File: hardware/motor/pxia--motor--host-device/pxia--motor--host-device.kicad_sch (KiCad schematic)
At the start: 12 parts, among them J1 RJ45, J2 Lolin D32 Pro 2.0.0 (ESP32) P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, J3 GENERIC_UART, J4 Lolin D32 Pro 2.0.0 (ESP32) P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, U1 Teensy4.0, U2 max3490eesa+T

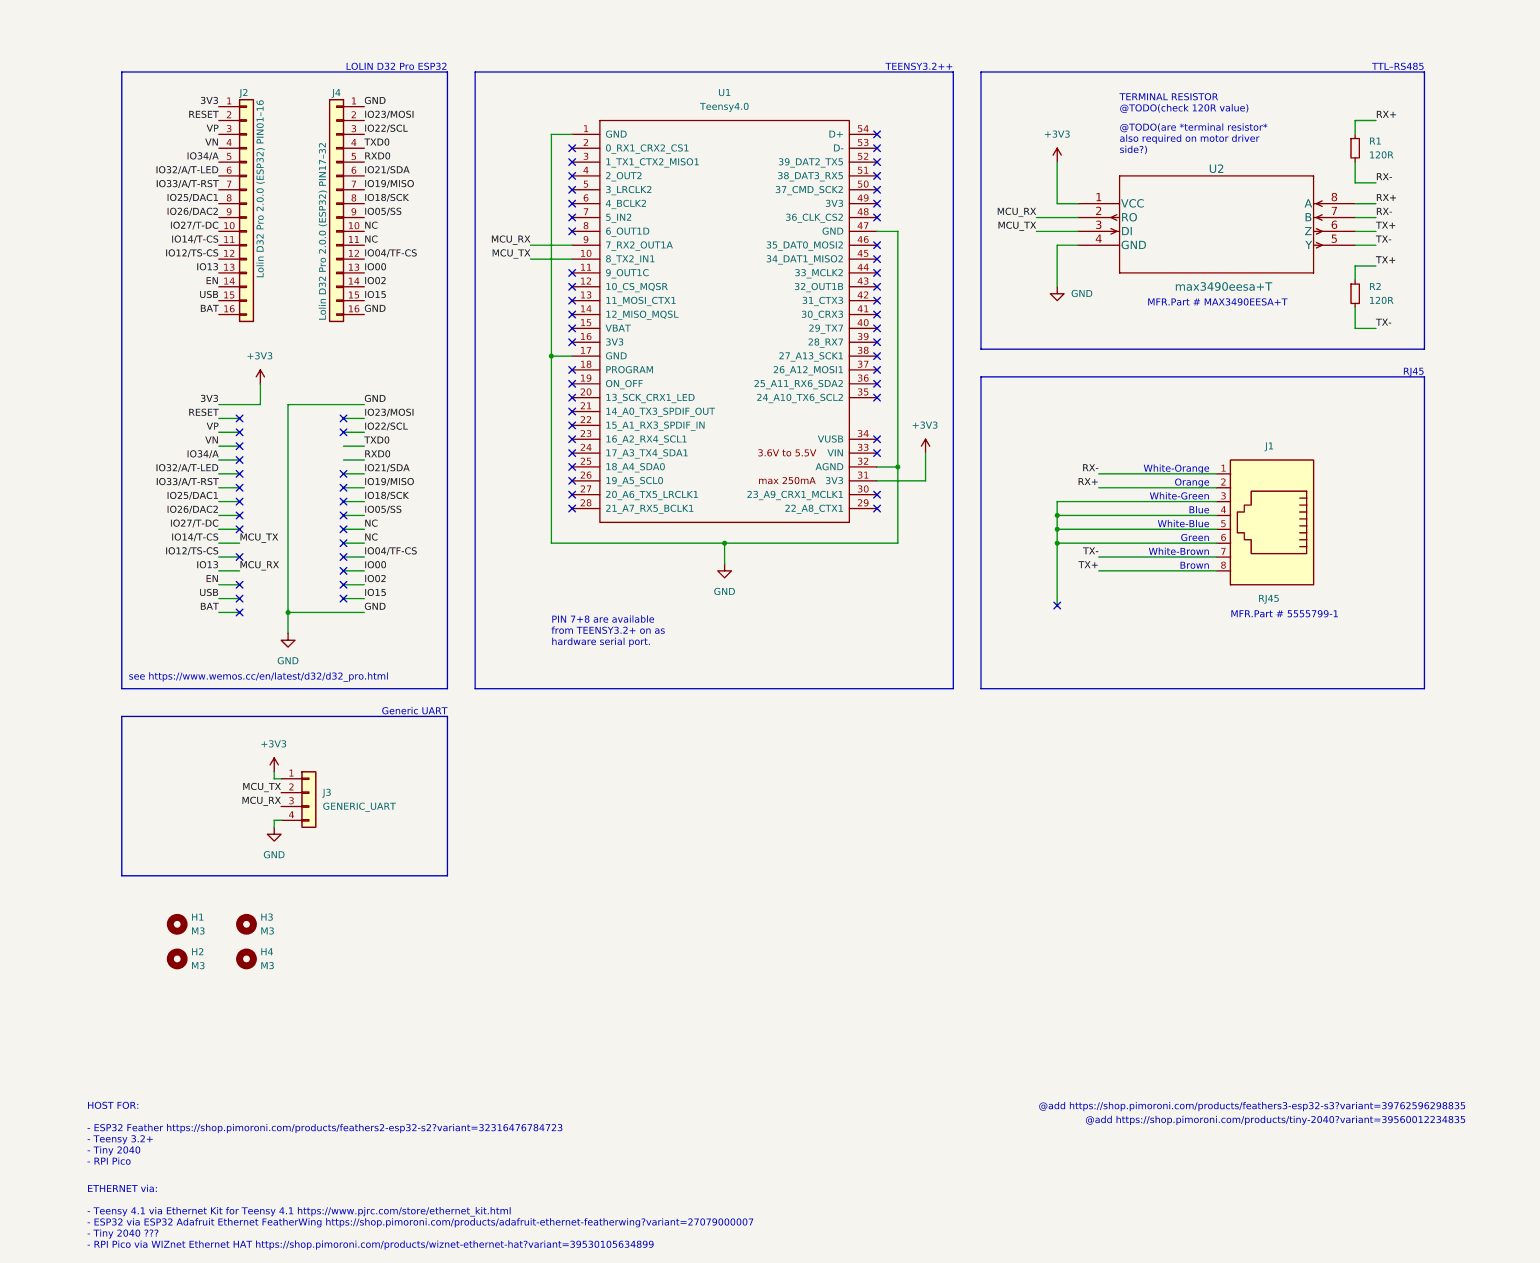
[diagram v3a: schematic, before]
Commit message: added PicoW, finished PCB layout
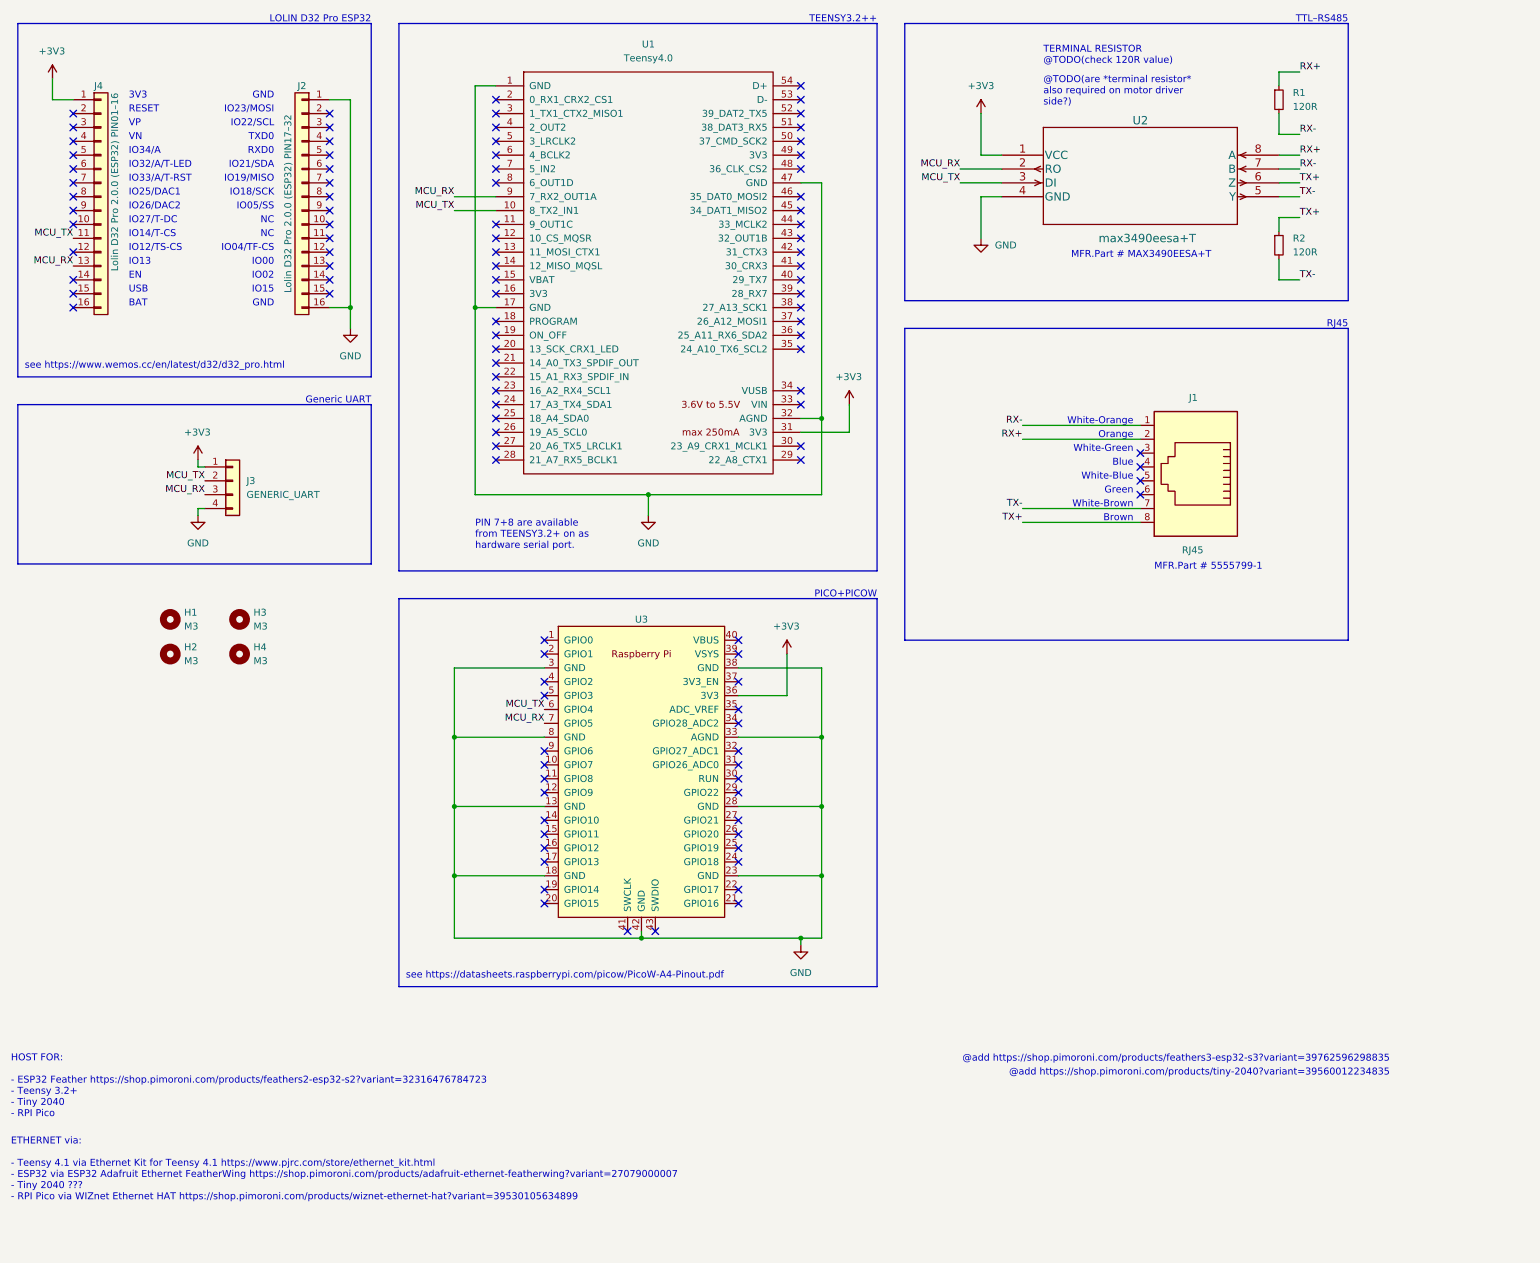
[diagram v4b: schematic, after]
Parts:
- added U3: (no value), symbol PicoW:PicoW
- J2: value Lolin D32 Pro 2.0.0 (ESP32) PIN01–16 -> Lolin D32 Pro 2.0.0 (ESP32) PIN17–32
- J4: value Lolin D32 Pro 2.0.0 (ESP32) PIN17–32 -> Lolin D32 Pro 2.0.0 (ESP32) PIN01–16
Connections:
- net BAT is gone; now on net GND: J2.16 (Pin_16)
- net +3V3: now also J4.1 (Pin_1), U3.36 (3V3); no longer J2.1 (Pin_1)
- net GND: now also J2.1 (Pin_1), U3.13 (GND), U3.18 (GND), U3.23 (GND), U3.28 (GND), U3.3 (GND), U3.33 (AGND), U3.38 (GND), U3.42 (GND), U3.8 (GND); no longer J4.1 (Pin_1), J4.16 (Pin_16)
- net EN: no longer names the net of J2.14 (Pin_14)
- net IO00 renamed MCU_RX
- net MCU_RX: now also J3.3 (Pin_3), U1.9 (7_RX2_OUT1A), U2.2 (RO), U3.7 (GPIO5)
- net IO02: no longer names the net of J4.14 (Pin_14)
- net IO04/TF-CS: no longer names the net of J4.12 (Pin_12)
- net IO05/SS: no longer names the net of J4.9 (Pin_9)
- net IO12/TS-CS: no longer names the net of J2.12 (Pin_12)
- removed net IO13: J2.13 (Pin_13), J3.3 (Pin_3), U1.9 (7_RX2_OUT1A), U2.2 (RO)
- net IO14/T-CS renamed MCU_TX
- net MCU_TX: now also J4.11 (Pin_11), U3.6 (GPIO4); no longer J2.11 (Pin_11)
- net IO15: no longer names the net of J4.15 (Pin_15)
- net IO18/SCK: no longer names the net of J4.8 (Pin_8)
- net IO19/MISO: no longer names the net of J4.7 (Pin_7)
- net IO21/SDA: no longer names the net of J4.6 (Pin_6)
- net IO22/SCL: no longer names the net of J4.3 (Pin_3)
- net IO23/MOSI: no longer names the net of J4.2 (Pin_2)
- net IO25/DAC1: no longer names the net of J2.8 (Pin_8)
- net IO26/DAC2: no longer names the net of J2.9 (Pin_9)
- net IO27/T-DC: no longer names the net of J2.10 (Pin_10)
- net IO32/A/T-LED: no longer names the net of J2.6 (Pin_6)
- net IO33/A/T-RST: no longer names the net of J2.7 (Pin_7)
- net IO34/A: no longer names the net of J2.5 (Pin_5)
- net NC: no longer names the net of J4.10 (Pin_10)
- net NC: no longer J4.11 (Pin_11)
- net RESET: no longer names the net of J2.2 (Pin_2)
- net RXD0: no longer names the net of J4.5 (Pin_5)
- net TXD0: no longer names the net of J4.4 (Pin_4)
- net USB: no longer names the net of J2.15 (Pin_15)
- net VN: no longer names the net of J2.4 (Pin_4)
- net VP: no longer names the net of J2.3 (Pin_3)
- now unconnected: J1.3, J1.4, J1.5, J1.6
- no-connect marks 73 -> 109
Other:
- note added: "3V3"
- note added: "BAT"
- note added: "EN"
- note added: "GND"
- note added: "IO00"
- note added: "IO02"
- note added: "IO04/TF-CS"
- note added: "IO05/SS"
- note added: "IO12/TS-CS"
- note added: "IO13"
- note added: "IO14/T-CS"
- note added: "IO15"
- note added: "IO18/SCK"
- note added: "IO19/MISO"
- note added: "IO21/SDA"
- note added: "IO22/SCL"
- note added: "IO23/MOSI"
- note added: "IO25/DAC1"
- note added: "IO26/DAC2"
- note added: "IO27/T-DC"
- note added: "IO32/A/T-LED"
- note added: "IO33/A/T-RST"
- note added: "IO34/A"
- note added: "NC"
- note added: "PICO+PICOW"
- note added: "RESET"
- note added: "RXD0"
- note added: "TXD0"
- note added: "USB"
- note added: "VN"
- note added: "VP"
- note added: "see https://datasheets.raspberrypi.com/picow/PicoW-A4-Pinout.pdf"
- moved on the sheet: H1, H2, H3, H4, J1, J3, R1, R2, U1, U2

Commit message: cleaned up, production ready
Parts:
- added J5: RJ45, Connector_RJ:RJ45_OST_PJ012-8P8CX_Vertical, symbol Connector:RJ45
- H1, H2, H3, H4, J2, J3, J4, U1: LCSC (none) -> DNF
- J1: LCSC (none) -> C305983
- R1, R2: LCSC (none) -> C114244
- U2: value max3490eesa+T -> (none); footprint Package_SO:SOIC-8_3.9x4.9mm_P1.27mm -> (none); LCSC (none) -> C23404
- U3: value (none) -> PicoW; footprint (none) -> PicoW:RPi_PicoW_SMD_TH; LCSC (none) -> DNF
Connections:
- net RX+: now also J5.2
- net RX-: now also J5.1
- net TX+: now also J5.8
- net TX-: now also J5.7
- no-connect marks 109 -> 113

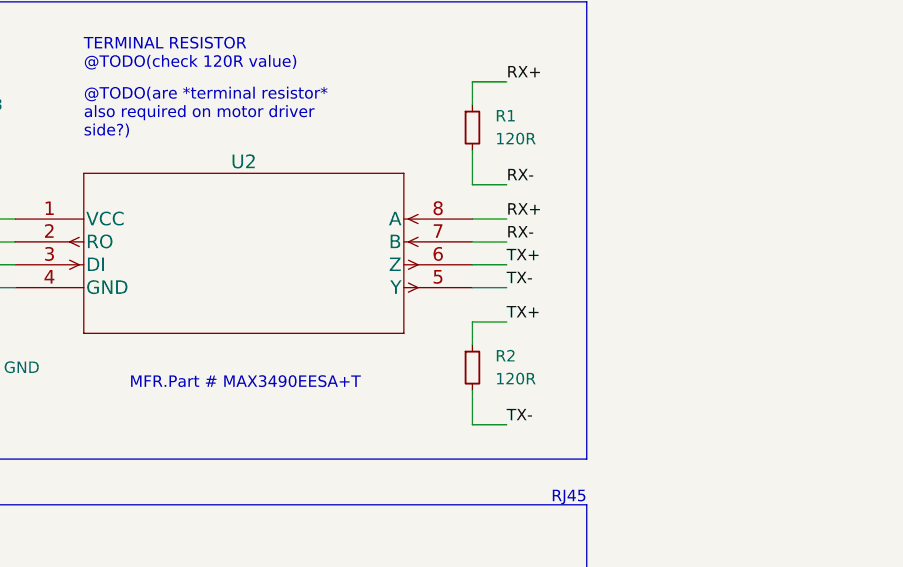
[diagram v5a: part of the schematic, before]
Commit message: updated documentation, fixed wrong wiring
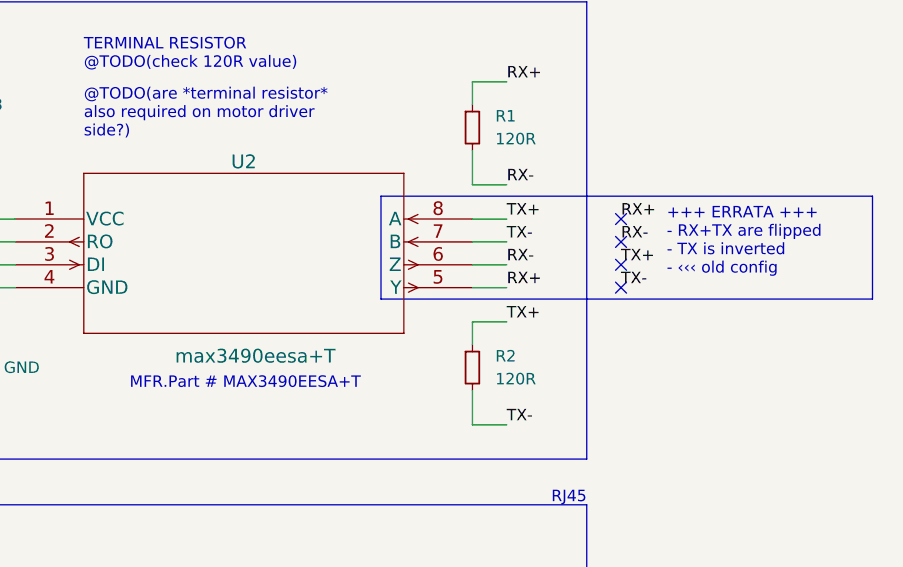
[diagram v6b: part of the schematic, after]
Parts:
- U2: value (none) -> max3490eesa+T; footprint (none) -> Package_SO:SOIC-8_3.9x4.9mm_P1.27mm
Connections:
- net RX+: now also U2.5 (Y); no longer U2.8 (A)
- net RX-: now also U2.6 (Z); no longer U2.7 (B)
- net TX+: now also U2.8 (A); no longer U2.6 (Z)
- net TX-: now also U2.7 (B); no longer U2.5 (Y)
- no-connect marks 113 -> 117
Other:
- note added: "+++ ERRATA +++ - RX+TX are flipped - TX is inverted - ‹‹‹ old config"
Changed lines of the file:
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@@
   (no_connect (at 101.6 93.98))
   (no_connect (at 219.71 102.87))
+  (no_connect (at 261.62 40.64))
   (no_connect (at 101.6 81.28))
   (no_connect (at 146.05 144.78))
@@
   (no_connect (at 101.6 40.64))
   (no_connect (at 71.12 66.04))
+  (no_connect (at 261.62 45.72))
   (no_connect (at 101.6 86.36))
   (no_connect (at 110.49 132.08))
@@
   (no_connect (at 110.49 167.64))
   (no_connect (at 146.05 167.64))
+  (no_connect (at 261.62 43.18))
   (no_connect (at 24.13 35.56))
   (no_connect (at 219.71 97.79))
@@
   (no_connect (at 101.6 30.48))
   (no_connect (at 101.6 71.12))
+  (no_connect (at 261.62 48.26))
   (no_connect (at 101.6 66.04))
   (no_connect (at 146.05 142.24))
@@
     (stroke (width 0) (type default) (color 0 0 0 0))
   )
+  (polyline (pts (xy 234.95 49.53) (xy 289.56 49.53))
+    (stroke (width 0) (type default) (color 0 0 0 0))
+  )
   (wire (pts (xy 46.99 105.41) (xy 46.99 106.68))
     (stroke (width 0) (type default) (color 0 0 0 0))
@@
     (stroke (width 0) (type default) (color 0 0 0 0))
   )
+  (polyline (pts (xy 289.56 49.53) (xy 289.56 38.1))
+    (stroke (width 0) (type default) (color 0 0 0 0))
+  )
   (wire (pts (xy 154.94 132.08) (xy 154.94 139.7))
     (stroke (width 0) (type default) (color 0 0 0 0))
@@
     (stroke (width 0) (type default) (color 0 0 0 0))
   )
+  (polyline (pts (xy 234.95 38.1) (xy 289.56 38.1))
+    (stroke (width 0) (type default) (color 0 0 0 0))
+  )
   (wire (pts (xy 245.11 59.69) (xy 245.11 63.5))
     (stroke (width 0) (type default) (color 0 0 0 0))
@@
   )
   (polyline (pts (xy 176.53 161.29) (xy 257.81 161.29))
+    (stroke (width 0) (type default) (color 0 0 0 0))
+  )
+  (polyline (pts (xy 234.95 38.1) (xy 234.95 49.53))
     (stroke (width 0) (type default) (color 0 0 0 0))
   )
@@
     (effects (font (size 1.27 1.27)) (justify right bottom))
   )
+  (text "+++ ERRATA +++\n- RX+TX are flipped\n- TX is inverted\n- ‹‹‹ old config"
+    (at 266.7 46.99 0)
+    (effects (font (size 1.27 1.27)) (justify left bottom))
+  )
   (text "Blue" (at 218.44 97.79 180)
     (effects (font (size 1.27 1.27)) (justify right bottom))
@@
     (effects (font (size 1.27 1.27)) (justify right bottom))
   )
-  (label "TX+" (at 248.92 45.72 0)
+  (label "TX+" (at 261.62 45.72 0)
     (effects (font (size 1.27 1.27)) (justify left bottom))
   )
@@
     (effects (font (size 1.27 1.27)) (justify right bottom))
   )
+  (label "TX-" (at 248.92 43.18 0)
+    (effects (font (size 1.27 1.27)) (justify left bottom))
+  )
   (label "RX+" (at 248.92 25.4 0)
     (effects (font (size 1.27 1.27)) (justify left bottom))
@@
     (effects (font (size 1.27 1.27)) (justify left bottom))
   )
-  (label "TX-" (at 248.92 48.26 0)
+  (label "TX-" (at 261.62 48.26 0)
+    (effects (font (size 1.27 1.27)) (justify left bottom))
+  )
+  (label "RX+" (at 248.92 48.26 0)
     (effects (font (size 1.27 1.27)) (justify left bottom))
   )
@@
     (effects (font (size 1.27 1.27)) (justify right bottom))
   )
+  (label "TX+" (at 248.92 40.64 0)
+    (effects (font (size 1.27 1.27)) (justify left bottom))
+  )
   (label "MCU_RX" (at 186.69 43.18 180)
     (effects (font (size 1.27 1.27)) (justify right bottom))
@@
     (effects (font (size 1.27 1.27)) (justify right bottom))
   )
+  (label "RX-" (at 248.92 45.72 0)
+    (effects (font (size 1.27 1.27)) (justify left bottom))
+  )
   (label "RX+" (at 198.12 92.71 180)
     (effects (font (size 1.27 1.27)) (justify right bottom))
   )
-  (label "RX-" (at 248.92 43.18 0)
+  (label "RX-" (at 261.62 43.18 0)
     (effects (font (size 1.27 1.27)) (justify left bottom))
   )
@@
     (effects (font (size 1.27 1.27)) (justify left bottom))
   )
-  (label "RX+" (at 248.92 40.64 0)
+  (label "RX+" (at 261.62 40.64 0)
     (effects (font (size 1.27 1.27)) (justify left bottom))
   )
@@
       (effects (font (size 1.524 1.524)))
     )
-    (property "Value" "" (id 1) (at 220.98 55.88 0)
+    (property "Value" "max3490eesa+T" (id 1) (at 220.98 55.88 0)
       (effects (font (size 1.524 1.524)))
     )
-    (property "Footprint" "" (id 2) (at 219.71 34.544 0)
+    (property "Footprint" "Package_SO:SOIC-8_3.9x4.9mm_P1.27mm" (id 2) (at 219.71 34.544 0)
       (effects (font (size 1.524 1.524)) hide)
     )
